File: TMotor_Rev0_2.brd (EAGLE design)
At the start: 91.5 x 74.3 mm, 78 parts, among them J1 5015680507, J10 5015680207, J2 5015680507, J7 5015680207, J8 5015680207, J9 5015680207, U1 INA125U, U2 INA125U, U3 INA125U, U4 INA125U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

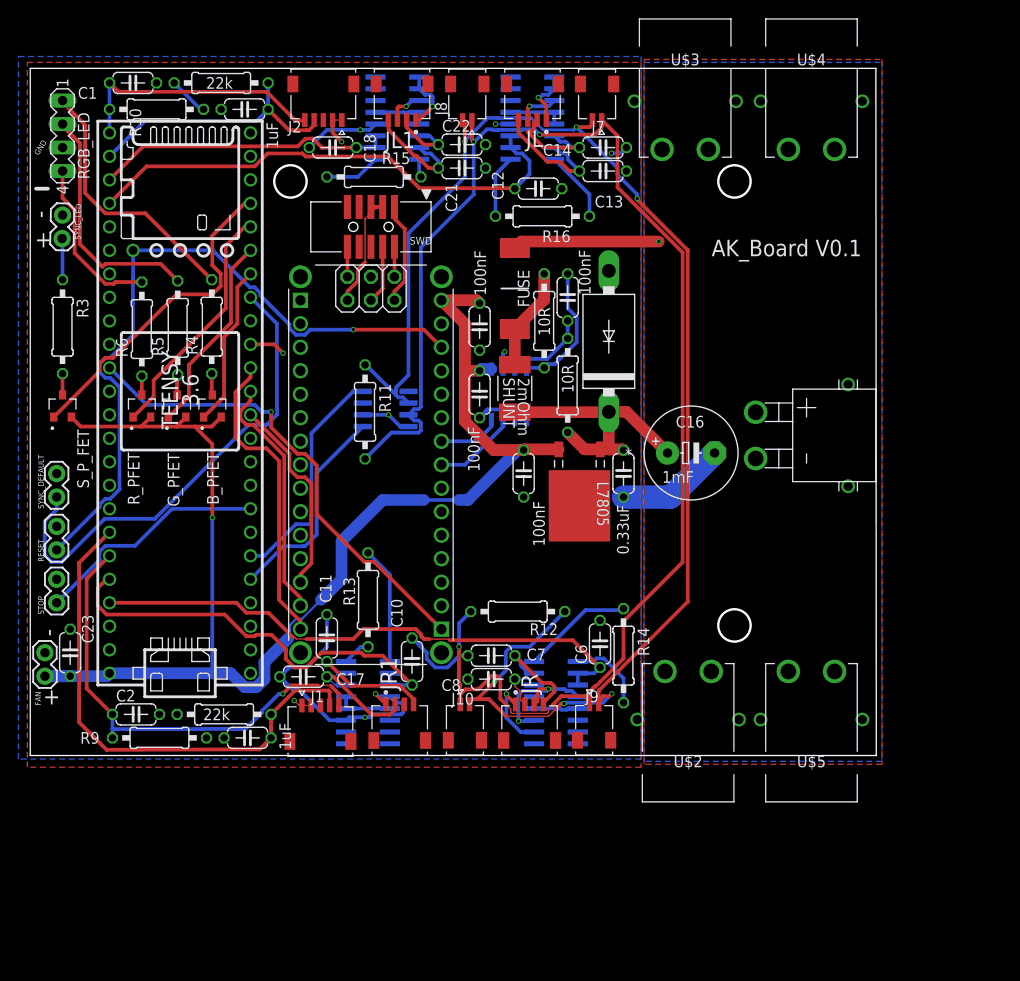
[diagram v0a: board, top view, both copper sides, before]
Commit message: updated LED power
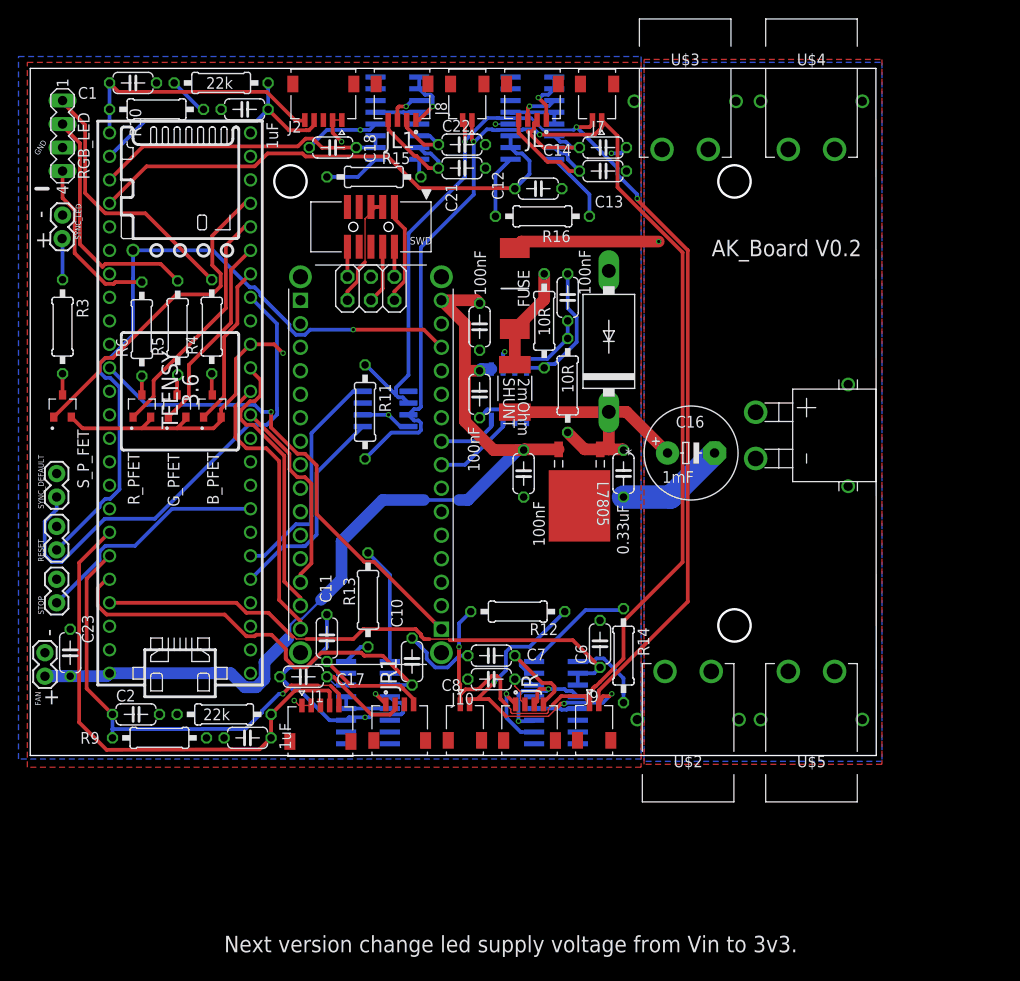
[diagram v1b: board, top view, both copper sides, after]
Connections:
- net 3.3V: now also B_PFET.2, G_PFET.2, R_PFET.2, S_P_FET.2
- net MISO: now also U$1.11/MOSI; no longer U$1.12/MISO
- net MOSI: now also U$1.12/MISO; no longer U$1.11/MOSI
- net VIN: no longer B_PFET.2, G_PFET.2, R_PFET.2, S_P_FET.2
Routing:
- net VIN: track 150.3 -> 102.9 mm, vias 1 -> 0
- net 3.3V: track 31.8 -> 61.6 mm
- net MOSI: track 26.7 -> 30.5 mm
- net MISO: track 33.1 -> 30.6 mm
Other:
- board text added: "AK_Board V0.2"
- board text added: "Next version change led supply voltage from Vin to 3v3."
- board text removed: "AK_Board V0.1"
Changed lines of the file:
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@@
 <layer number="20" name="Dimension" color="24" fill="1" visible="yes" active="yes"/>
 <layer number="21" name="tPlace" color="7" fill="1" visible="yes" active="yes"/>
-<layer number="22" name="bPlace" color="7" fill="1" visible="no" active="yes"/>
+<layer number="22" name="bPlace" color="7" fill="1" visible="yes" active="yes"/>
 <layer number="23" name="tOrigins" color="15" fill="1" visible="yes" active="yes"/>
 <layer number="24" name="bOrigins" color="15" fill="1" visible="yes" active="yes"/>
@@
 <circle x="42.475" y="69.365" radius="1.75" width="0.254" layer="20"/>
 <circle x="42.475" y="21.365" radius="1.75" width="0.254" layer="20"/>
-<text x="40.005" y="61.2775" size="1.778" layer="21">AK_Board V0.1</text>
+<text x="40.005" y="61.2775" size="1.778" layer="21">AK_Board V0.2</text>
 <text x="-32.258" y="12.827" size="1.778" layer="121">+</text>
 <text x="-30.861" y="20.193" size="1.778" layer="121" rot="R90">-</text>
@@
 <wire x1="-33.02" y1="68.58" x2="-31.75" y2="68.58" width="0.4064" layer="121"/>
 <text x="-31.75" y="65.405" size="1.778" layer="121" rot="R90">-</text>
+<text x="-12.7" y="-13.97" size="1.778" layer="121">Next version change led supply voltage from Vin to 3v3.</text>
 </plain>
 <attributes>
@@
 <contactref element="L7805" pad="2"/>
 <contactref element="C15" pad="1"/>
-<contactref element="B_PFET" pad="2"/>
-<contactref element="G_PFET" pad="2"/>
-<contactref element="R_PFET" pad="2"/>
-<contactref element="S_P_FET" pad="2"/>
 <contactref element="U$1" pad="VIN"/>
 <wire x1="10.795" y1="56.515" x2="13.335" y2="53.975" width="1.27" layer="1"/>
@@
 <wire x1="0" y1="26.3525" x2="0" y2="30.48" width="1.27" layer="16"/>
 <wire x1="0" y1="30.48" x2="4.445" y2="34.925" width="1.27" layer="16"/>
-<wire x1="-29.2125" y1="43.885" x2="-28.19" y2="42.8625" width="0.4064" layer="1"/>
-<wire x1="-13.02" y1="43.885" x2="-14.0425" y2="42.8625" width="0.4064" layer="1"/>
-<wire x1="-28.19" y1="42.8625" x2="-21.6625" y2="42.8625" width="0.4064" layer="1"/>
-<wire x1="-21.6625" y1="42.8625" x2="-17.8525" y2="42.8625" width="0.4064" layer="1"/>
-<wire x1="-17.8525" y1="42.8625" x2="-15.875" y2="42.8625" width="0.4064" layer="1"/>
-<wire x1="-15.875" y1="42.8625" x2="-14.0425" y2="42.8625" width="0.4064" layer="1"/>
-<wire x1="-16.83" y1="43.885" x2="-17.8525" y2="42.8625" width="0.4064" layer="1"/>
-<wire x1="-20.64" y1="43.885" x2="-21.6625" y2="42.8625" width="0.4064" layer="1"/>
 <wire x1="10.795" y1="56.515" x2="14.605" y2="56.515" width="1.27" layer="1"/>
 <wire x1="14.605" y1="56.515" x2="14.9225" y2="56.1975" width="1.27" layer="1"/>
@@
 <wire x1="14.9225" y1="48.895" x2="15.10665" y2="49.07915" width="1.27" layer="16"/>
 <wire x1="15.10665" y1="49.07915" x2="16.1925" y2="49.07915" width="1.27" layer="16"/>
-<wire x1="-13.97" y1="40.9575" x2="-13.97" y2="33.02" width="0.4064" layer="1"/>
-<via x="-13.97" y="33.02" extent="1-16" drill="0.35"/>
-<wire x1="-13.97" y1="33.02" x2="-13.97" y2="16.1925" width="0.4064" layer="16"/>
-<wire x1="-15.875" y1="42.8625" x2="-13.97" y2="40.9575" width="0.4064" layer="1"/>
 <contactref element="C23" pad="2"/>
 <wire x1="-29.337" y1="15.875" x2="-32.0675" y2="15.875" width="1.27" layer="16"/>
@@
 <wire x1="3.6731" y1="13.97" x2="4.7865" y2="12.8566" width="0.4064" layer="1"/>
 <wire x1="4.7865" y1="12.8566" x2="4.7865" y2="12.827" width="0.4064" layer="1"/>
+<contactref element="S_P_FET" pad="2"/>
+<contactref element="B_PFET" pad="2"/>
+<contactref element="G_PFET" pad="2"/>
+<contactref element="R_PFET" pad="2"/>
+<wire x1="-29.2125" y1="43.885" x2="-27.9995" y2="42.672" width="0.4064" layer="1"/>
+<wire x1="-27.9995" y1="42.672" x2="-21.59" y2="42.672" width="0.4064" layer="1"/>
+<wire x1="-21.59" y1="42.672" x2="-17.78" y2="42.672" width="0.4064" layer="1"/>
+<wire x1="-17.78" y1="42.672" x2="-13.843" y2="42.672" width="0.4064" layer="1"/>
+<wire x1="-13.843" y1="42.672" x2="-13.02" y2="43.495" width="0.4064" layer="1"/>
+<wire x1="-13.02" y1="43.495" x2="-13.02" y2="43.885" width="0.4064" layer="1"/>
+<wire x1="-13.02" y1="43.885" x2="-13.02" y2="44.765" width="0.4064" layer="1"/>
+<wire x1="-11.43" y1="50.165" x2="-9.8425" y2="51.7525" width="0.4064" layer="1"/>
+<wire x1="-13.02" y1="44.765" x2="-11.43" y2="46.355" width="0.4064" layer="1"/>
+<wire x1="-11.43" y1="46.355" x2="-11.43" y2="50.165" width="0.4064" layer="1"/>
+<wire x1="-20.64" y1="43.885" x2="-20.64" y2="43.622" width="0.4064" layer="1"/>
+<wire x1="-20.64" y1="43.622" x2="-21.59" y2="42.672" width="0.4064" layer="1"/>
+<wire x1="-16.83" y1="43.885" x2="-16.83" y2="43.622" width="0.4064" layer="1"/>
+<wire x1="-16.83" y1="43.622" x2="-17.78" y2="42.672" width="0.4064" layer="1"/>
+<wire x1="9.8425" y1="77.47" x2="21.2725" y2="78.4225" width="0" layer="19" extent="1-1"/>
+<wire x1="0.0315" y1="75.9995" x2="8.0405" y2="76.0095" width="0" layer="19" extent="1-1"/>
+<wire x1="-6.3274" y1="50.8" x2="0" y2="73.66" width="0" layer="19" extent="1-1"/>
+<wire x1="2.2925" y1="45.4025" x2="-6.3274" y2="50.8" width="0" layer="19" extent="16-16"/>
+<wire x1="3.6731" y1="13.97" x2="2.2925" y2="45.4025" width="0" layer="19" extent="16-16"/>
+<wire x1="0.4953" y1="9.8425" x2="3.6731" y2="13.97" width="0" layer="19" extent="16-16"/>
+<wire x1="0.4953" y1="8.5725" x2="0.4953" y2="9.8425" width="0" layer="19" extent="16-16"/>
+<wire x1="-3.286" y1="12.715" x2="0.4953" y2="9.8425" width="0" layer="19" extent="1-16"/>
+<wire x1="17.8252" y1="13.97" x2="4.7865" y2="12.827" width="0" layer="19" extent="1-1"/>
+<wire x1="20.8153" y1="8.5725" x2="20.8153" y2="9.8425" width="0" layer="19" extent="16-16"/>
 </signal>
 <signal name="NANO_CS">
@@
 <signal name="MOSI">
 <contactref element="USB" pad="B14"/>
-<contactref element="U$1" pad="11/MOSI"/>
-<wire x1="-10.922" y1="44.57964375" x2="-10.922" y2="43.68535625" width="0.4064" layer="1"/>
+<wire x1="-10.922" y1="44.45" x2="-10.922" y2="43.68535625" width="0.4064" layer="1"/>
 <wire x1="-10.922" y1="43.68535625" x2="-10.28964375" y2="43.053" width="0.4064" layer="1"/>
 <wire x1="-10.28964375" y1="43.053" x2="-9.55326875" y2="43.053" width="0.4064" layer="1"/>
-<wire x1="-9.8425" y1="46.6725" x2="-9.8425" y2="45.65914375" width="0.4064" layer="1"/>
-<wire x1="-9.8425" y1="45.65914375" x2="-10.922" y2="44.57964375" width="0.4064" layer="1"/>
 <wire x1="-4.445" y1="24.35476875" x2="-4.445" y2="23.495" width="0.4064" layer="1"/>
 <wire x1="-6.1919" y1="39.69163125" x2="-6.1919" y2="26.10166875" width="0.4064" layer="1"/>
 <wire x1="-6.1919" y1="26.10166875" x2="-4.445" y2="24.35476875" width="0.4064" layer="1"/>
 <wire x1="-9.55326875" y1="43.053" x2="-6.1919" y2="39.69163125" width="0.4064" layer="1"/>
+<contactref element="U$1" pad="12/MISO"/>
+<wire x1="-9.8425" y1="48.9894125" x2="-9.8425" y2="49.2125" width="0.4064" layer="1"/>
+<wire x1="-8.763" y1="46.22535625" x2="-8.763" y2="47.9099125" width="0.4064" layer="1"/>
+<wire x1="-8.763" y1="47.9099125" x2="-9.8425" y2="48.9894125" width="0.4064" layer="1"/>
+<wire x1="-10.922" y1="44.45" x2="-10.922" y2="44.57964375" width="0.4064" layer="1"/>
+<wire x1="-9.39535625" y1="45.593" x2="-8.763" y2="46.22535625" width="0.4064" layer="1"/>
+<wire x1="-10.922" y1="44.57964375" x2="-9.90864375" y2="45.593" width="0.4064" layer="1"/>
+<wire x1="-9.90864375" y1="45.593" x2="-9.39535625" y2="45.593" width="0.4064" layer="1"/>
 </signal>
 <signal name="TRQ_AMP_L">
@@
 <signal name="MISO">
 <contactref element="USB" pad="B15"/>
-<contactref element="U$1" pad="12/MISO"/>
-<wire x1="-9.8425" y1="49.2125" x2="-9.8425" y2="48.19914375" width="0.4064" layer="1"/>
-<wire x1="-9.8425" y1="48.19914375" x2="-11.4808" y2="46.56084375" width="0.4064" layer="1"/>
 <wire x1="-10.28964375" y1="40.513" x2="-8.128" y2="40.513" width="0.4064" layer="1"/>
-<wire x1="-11.4808" y1="41.70415625" x2="-10.28964375" y2="40.513" width="0.4064" layer="1"/>
+<wire x1="-10.28964375" y1="40.513" x2="-11.4808" y2="41.70415625" width="0.4064" layer="1"/>
 <wire x1="-4.445" y1="21.81476875" x2="-4.445" y2="20.955" width="0.4064" layer="1"/>
 <wire x1="-6.7507" y1="39.1357" x2="-6.7507" y2="24.12046875" width="0.4064" layer="1"/>
 <wire x1="-6.7507" y1="24.12046875" x2="-4.445" y2="21.81476875" width="0.4064" layer="1"/>
-<wire x1="-11.4808" y1="46.56084375" x2="-11.4808" y2="41.70415625" width="0.4064" layer="1"/>
 <wire x1="-8.128" y1="40.513" x2="-6.7507" y2="39.1357" width="0.4064" layer="1"/>
+<contactref element="U$1" pad="11/MOSI"/>
+<wire x1="-11.4808" y1="41.70415625" x2="-11.4808" y2="45.0342" width="0.4064" layer="1"/>
+<wire x1="-11.4808" y1="45.0342" x2="-9.8425" y2="46.6725" width="0.4064" layer="1"/>
 </signal>
 <signal name="SCK">
